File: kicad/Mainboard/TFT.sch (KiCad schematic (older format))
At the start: 2 parts, among them J6 55746-0871, Q1 BSS138

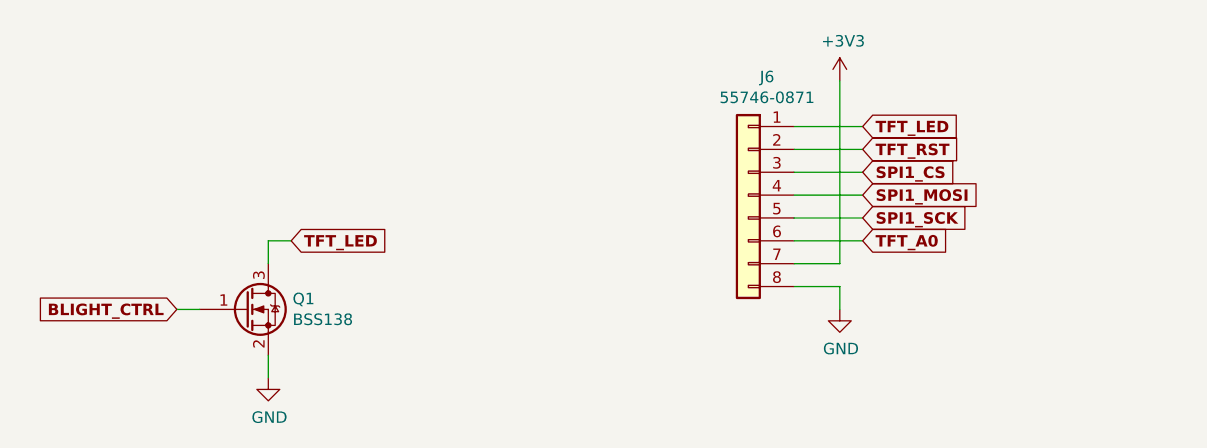
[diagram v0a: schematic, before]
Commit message: Add files via upload
* replaced Q7 with BSS138
* new HMI connector (for keypad and display)
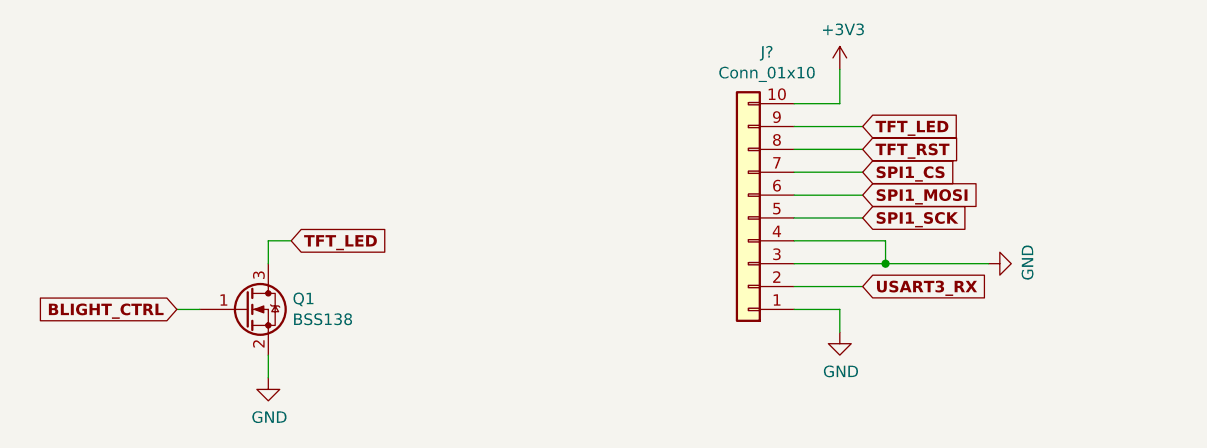
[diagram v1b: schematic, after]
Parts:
- removed J6: 55746-0871, symbol Mainboard-rescue:Conn_01x08-conn
- added J?: Conn_01x10, symbol Connector_Generic:Conn_01x10
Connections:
- net +3V3: now also J?.10 (Pin_10)
- net GND: now also J?.1 (Pin_1), J?.3 (Pin_3), J?.4 (Pin_4)
- net SPI1_CS: now also J?.7 (Pin_7)
- net SPI1_MOSI: now also J?.6 (Pin_6)
- net SPI1_SCK: now also J?.5 (Pin_5)
- net TFT_LED: now also J?.9 (Pin_9)
- net TFT_RST: now also J?.8 (Pin_8)
- new net USART3_RX: J?.2 (Pin_2)
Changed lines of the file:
@@
 EESchema Schematic File Version 4
+LIBS:Mainboard-cache
 EELAYER 30 0
 EELAYER END
@@
 encoding utf-8
 Sheet 4 7
-Title "Display Connector"
+Title "HMI Board Connector"
 Date ""
 Rev ""
@@
 Text GLabel 3600 3800 2    50   Input ~ 10
 TFT_LED
-$Comp
-L Mainboard-rescue:Conn_01x08-conn J6
-U 1 1 5DF0C355
-P 5600 3600
-F 0 "J6" H 5518 4117 50  0000 C CNN
-F 1 "55746-0871" H 5518 4026 50  0000 C CNN
-F 2 "" H 5600 3600 50  0001 C CNN
-F 3 "~" H 5600 3600 50  0001 C CNN
-	1    5600 3600
-	-1   0    0    -1
-$EndComp
 Text GLabel 6100 3300 2    50   Input ~ 10
 TFT_LED
@@
 Text GLabel 6100 3700 2    50   Input ~ 10
 SPI1_SCK
-Text GLabel 6100 3800 2    50   Input ~ 10
-TFT_A0
 Wire Wire Line
 	5800 3300 6100 3300
@@
 	5800 3700 6100 3700
 Wire Wire Line
-	5800 3800 6100 3800
+	5800 3200 6000 3200
 Wire Wire Line
-	5800 3900 6000 3900
-Wire Wire Line
-	6000 3900 6000 3100
+	6000 3200 6000 3050
 $Comp
 L power:+3V3 #PWR049
 U 1 1 5DF0DB74
-P 6000 3100
-F 0 "#PWR049" H 6000 2950 50  0001 C CNN
-F 1 "+3V3" H 6015 3273 50  0000 C CNN
-F 2 "" H 6000 3100 50  0001 C CNN
-F 3 "" H 6000 3100 50  0001 C CNN
-	1    6000 3100
+P 6000 3050
+F 0 "#PWR049" H 6000 2900 50  0001 C CNN
+F 1 "+3V3" H 6015 3223 50  0000 C CNN
+F 2 "" H 6000 3050 50  0001 C CNN
+F 3 "" H 6000 3050 50  0001 C CNN
+	1    6000 3050
 	1    0    0    -1
 $EndComp
 Wire Wire Line
-	5800 4000 6000 4000
+	5800 4100 6000 4100
 Wire Wire Line
-	6000 4000 6000 4100
+	6000 4100 6000 4200
 $Comp
 L power:GND #PWR050
 U 1 1 5DF0E0D2
-P 6000 4100
-F 0 "#PWR050" H 6000 3850 50  0001 C CNN
-F 1 "GND" H 6005 3927 50  0000 C CNN
-F 2 "" H 6000 4100 50  0001 C CNN
-F 3 "" H 6000 4100 50  0001 C CNN
-	1    6000 4100
+P 6000 4200
+F 0 "#PWR050" H 6000 3950 50  0001 C CNN
+F 1 "GND" H 6005 4027 50  0000 C CNN
+F 2 "" H 6000 4200 50  0001 C CNN
+F 3 "" H 6000 4200 50  0001 C CNN
+	1    6000 4200
 	1    0    0    -1
 $EndComp
+Wire Wire Line
+	5800 4000 6100 4000
+Text GLabel 6100 4000 2    50   Input ~ 10
+USART3_RX
+$Comp
+L power:GND #PWR?
+U 1 1 5E1E62B4
+P 6650 3900
+F 0 "#PWR?" H 6650 3650 50  0001 C CNN
+F 1 "GND" H 6655 3727 50  0000 C CNN
+F 2 "" H 6650 3900 50  0001 C CNN
+F 3 "" H 6650 3900 50  0001 C CNN
+	1    6650 3900
+	0    -1   -1   0
+$EndComp
+Wire Wire Line
+	5800 3900 6200 3900
+Wire Wire Line
+	5800 3800 6200 3800
+Wire Wire Line
+	6200 3800 6200 3900
+Connection ~ 6200 3900
+Wire Wire Line
+	6200 3900 6650 3900
+$Comp
+L Connector_Generic:Conn_01x10 J?
+U 1 1 5E1EAE64
+P 5600 3700
+F 0 "J?" H 5518 2975 50  0000 C CNN
+F 1 "Conn_01x10" H 5518 3066 50  0000 C CNN
+F 2 "" H 5600 3700 50  0001 C CNN
+F 3 "~" H 5600 3700 50  0001 C CNN
+	1    5600 3700
+	-1   0    0    1
+$EndComp
 $EndSCHEMATC

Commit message: Add files via upload
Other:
- moved on the sheet: J?, Q1
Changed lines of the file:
@@
 L Mainboard-rescue:BSS138-transistors Q1
 U 1 1 5DF0AD3D
-P 3400 4100
-F 0 "Q1" H 3606 4146 50  0000 L CNN
-F 1 "BSS138" H 3606 4055 50  0000 L CNN
-F 2 "TO_SOT_Packages_SMD:SOT-23" H 3600 4025 50  0001 L CIN
-F 3 "https://www.fairchildsemi.com/datasheets/BS/BSS138.pdf" H 3400 4100 50  0001 L CNN
-	1    3400 4100
+P 4300 3750
+F 0 "Q1" H 4506 3796 50  0000 L CNN
+F 1 "BSS138" H 4506 3705 50  0000 L CNN
+F 2 "TO_SOT_Packages_SMD:SOT-23" H 4500 3675 50  0001 L CIN
+F 3 "https://www.fairchildsemi.com/datasheets/BS/BSS138.pdf" H 4300 3750 50  0001 L CNN
+	1    4300 3750
 	1    0    0    -1
 $EndComp
@@
 L power:GND #PWR051
 U 1 1 5DF0BBF9
-P 3500 4400
-F 0 "#PWR051" H 3500 4150 50  0001 C CNN
-F 1 "GND" H 3505 4227 50  0000 C CNN
-F 2 "" H 3500 4400 50  0001 C CNN
-F 3 "" H 3500 4400 50  0001 C CNN
-	1    3500 4400
+P 4400 4050
+F 0 "#PWR051" H 4400 3800 50  0001 C CNN
+F 1 "GND" H 4405 3877 50  0000 C CNN
+F 2 "" H 4400 4050 50  0001 C CNN
+F 3 "" H 4400 4050 50  0001 C CNN
+	1    4400 4050
 	1    0    0    -1
 $EndComp
 Wire Wire Line
-	3500 4300 3500 4400
+	4400 3950 4400 4050
 Wire Wire Line
-	3200 4100 3100 4100
-Text GLabel 3100 4100 0    50   Input ~ 10
+	4100 3750 4000 3750
+Text GLabel 4000 3750 0    50   Input ~ 10
 BLIGHT_CTRL
 Wire Wire Line
-	3500 3900 3500 3800
+	4400 3550 4400 3450
 Wire Wire Line
-	3500 3800 3600 3800
-Text GLabel 3600 3800 2    50   Input ~ 10
+	4400 3450 4500 3450
+Text GLabel 4500 3450 2    50   Input ~ 10
 TFT_LED
-Text GLabel 6100 3300 2    50   Input ~ 10
+Text GLabel 6750 3450 2    50   Input ~ 10
 TFT_LED
-Text GLabel 6100 3400 2    50   Input ~ 10
+Text GLabel 6750 3550 2    50   Input ~ 10
 TFT_RST
-Text GLabel 6100 3500 2    50   Input ~ 10
+Text GLabel 6750 3650 2    50   Input ~ 10
 SPI1_CS
-Text GLabel 6100 3600 2    50   Input ~ 10
+Text GLabel 6750 3750 2    50   Input ~ 10
 SPI1_MOSI
-Text GLabel 6100 3700 2    50   Input ~ 10
+Text GLabel 6750 3850 2    50   Input ~ 10
 SPI1_SCK
 Wire Wire Line
-	5800 3300 6100 3300
+	6450 3450 6750 3450
 Wire Wire Line
-	5800 3400 6100 3400
+	6450 3550 6750 3550
 Wire Wire Line
-	5800 3500 6100 3500
+	6450 3650 6750 3650
 Wire Wire Line
-	5800 3600 6100 3600
+	6450 3750 6750 3750
 Wire Wire Line
-	5800 3700 6100 3700
+	6450 3850 6750 3850
 Wire Wire Line
-	5800 3200 6000 3200
+	6450 3350 6650 3350
 Wire Wire Line
-	6000 3200 6000 3050
+	6650 3350 6650 3200
 $Comp
 L power:+3V3 #PWR049
 U 1 1 5DF0DB74
-P 6000 3050
-F 0 "#PWR049" H 6000 2900 50  0001 C CNN
-F 1 "+3V3" H 6015 3223 50  0000 C CNN
-F 2 "" H 6000 3050 50  0001 C CNN
-F 3 "" H 6000 3050 50  0001 C CNN
-	1    6000 3050
+P 6650 3200
+F 0 "#PWR049" H 6650 3050 50  0001 C CNN
+F 1 "+3V3" H 6665 3373 50  0000 C CNN
+F 2 "" H 6650 3200 50  0001 C CNN
+F 3 "" H 6650 3200 50  0001 C CNN
+	1    6650 3200
 	1    0    0    -1
 $EndComp
 Wire Wire Line
-	5800 4100 6000 4100
+	6450 4250 6650 4250
 Wire Wire Line
-	6000 4100 6000 4200
+	6650 4250 6650 4350
 $Comp
 L power:GND #PWR050
 U 1 1 5DF0E0D2
-P 6000 4200
-F 0 "#PWR050" H 6000 3950 50  0001 C CNN
-F 1 "GND" H 6005 4027 50  0000 C CNN
-F 2 "" H 6000 4200 50  0001 C CNN
-F 3 "" H 6000 4200 50  0001 C CNN
-	1    6000 4200
+P 6650 4350
+F 0 "#PWR050" H 6650 4100 50  0001 C CNN
+F 1 "GND" H 6655 4177 50  0000 C CNN
+F 2 "" H 6650 4350 50  0001 C CNN
+F 3 "" H 6650 4350 50  0001 C CNN
+	1    6650 4350
 	1    0    0    -1
 $EndComp
 Wire Wire Line
-	5800 4000 6100 4000
-Text GLabel 6100 4000 2    50   Input ~ 10
+	6450 4150 6750 4150
+Text GLabel 6750 4150 2    50   Input ~ 10
 USART3_RX
 $Comp
 L power:GND #PWR?
 U 1 1 5E1E62B4
-P 6650 3900
-F 0 "#PWR?" H 6650 3650 50  0001 C CNN
-F 1 "GND" H 6655 3727 50  0000 C CNN
-F 2 "" H 6650 3900 50  0001 C CNN
-F 3 "" H 6650 3900 50  0001 C CNN
-	1    6650 3900
+P 7300 4050
+F 0 "#PWR?" H 7300 3800 50  0001 C CNN
+F 1 "GND" H 7305 3877 50  0000 C CNN
+F 2 "" H 7300 4050 50  0001 C CNN
+F 3 "" H 7300 4050 50  0001 C CNN
+	1    7300 4050
 	0    -1   -1   0
 $EndComp
 Wire Wire Line
-	5800 3900 6200 3900
+	6450 4050 6850 4050
 Wire Wire Line
-	5800 3800 6200 3800
+	6450 3950 6850 3950
 Wire Wire Line
-	6200 3800 6200 3900
-Connection ~ 6200 3900
+	6850 3950 6850 4050
+Connection ~ 6850 4050
 Wire Wire Line
-	6200 3900 6650 3900
+	6850 4050 7300 4050
 $Comp
 L Connector_Generic:Conn_01x10 J?
 U 1 1 5E1EAE64
-P 5600 3700
-F 0 "J?" H 5518 2975 50  0000 C CNN
-F 1 "Conn_01x10" H 5518 3066 50  0000 C CNN
-F 2 "" H 5600 3700 50  0001 C CNN
-F 3 "~" H 5600 3700 50  0001 C CNN
-	1    5600 3700
+P 6250 3850
+F 0 "J?" H 6168 3125 50  0000 C CNN
+F 1 "Conn_01x10" H 6168 3216 50  0000 C CNN
+F 2 "" H 6250 3850 50  0001 C CNN
+F 3 "~" H 6250 3850 50  0001 C CNN
+	1    6250 3850
 	-1   0    0    1
 $EndComp

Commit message: Add files via upload
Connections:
- net USART3_RX renamed UART7_RX
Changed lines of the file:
@@
 $Descr A4 11693 8268
 encoding utf-8
-Sheet 4 7
+Sheet 4 8
 Title "HMI Board Connector"
 Date ""
@@
 	6450 4150 6750 4150
 Text GLabel 6750 4150 2    50   Input ~ 10
-USART3_RX
+UART7_RX
 $Comp
 L power:GND #PWR?

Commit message: Annotated parts, again.
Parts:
- gave numbers to parts that had none: 1
- renumbered Q1 to Q2
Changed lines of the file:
@@
 EESchema Schematic File Version 4
-LIBS:Mainboard-cache
 EELAYER 30 0
 EELAYER END
@@
 $EndDescr
 $Comp
-L Mainboard-rescue:BSS138-transistors Q1
+L Mainboard-rescue:BSS138-transistors Q2
 U 1 1 5DF0AD3D
 P 4300 3750
-F 0 "Q1" H 4506 3796 50  0000 L CNN
+F 0 "Q2" H 4506 3796 50  0000 L CNN
 F 1 "BSS138" H 4506 3705 50  0000 L CNN
 F 2 "TO_SOT_Packages_SMD:SOT-23" H 4500 3675 50  0001 L CIN
@@
 	6650 3350 6650 3200
 $Comp
-L power:+3V3 #PWR049
+L power:+3V3 #PWR052
 U 1 1 5DF0DB74
 P 6650 3200
-F 0 "#PWR049" H 6650 3050 50  0001 C CNN
+F 0 "#PWR052" H 6650 3050 50  0001 C CNN
 F 1 "+3V3" H 6665 3373 50  0000 C CNN
 F 2 "" H 6650 3200 50  0001 C CNN
@@
 	6650 4250 6650 4350
 $Comp
-L power:GND #PWR050
+L power:GND #PWR053
 U 1 1 5DF0E0D2
 P 6650 4350
-F 0 "#PWR050" H 6650 4100 50  0001 C CNN
+F 0 "#PWR053" H 6650 4100 50  0001 C CNN
 F 1 "GND" H 6655 4177 50  0000 C CNN
 F 2 "" H 6650 4350 50  0001 C CNN
@@
 UART7_RX
 $Comp
-L power:GND #PWR?
+L power:GND #PWR054
 U 1 1 5E1E62B4
 P 7300 4050
-F 0 "#PWR?" H 7300 3800 50  0001 C CNN
+F 0 "#PWR054" H 7300 3800 50  0001 C CNN
 F 1 "GND" H 7305 3877 50  0000 C CNN
 F 2 "" H 7300 4050 50  0001 C CNN
@@
 	6850 4050 7300 4050
 $Comp
-L Connector_Generic:Conn_01x10 J?
+L Connector_Generic:Conn_01x10 J7
 U 1 1 5E1EAE64
 P 6250 3850
-F 0 "J?" H 6168 3125 50  0000 C CNN
+F 0 "J7" H 6168 3125 50  0000 C CNN
 F 1 "Conn_01x10" H 6168 3216 50  0000 C CNN
 F 2 "" H 6250 3850 50  0001 C CNN

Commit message: Started assigning footprints
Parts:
- J7: symbol Connector_Generic:Conn_01x10 -> Mainboard-rescue:Conn_01x10-Connector_Generic
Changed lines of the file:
@@
 	6850 4050 7300 4050
 $Comp
-L Connector_Generic:Conn_01x10 J7
+L Mainboard-rescue:Conn_01x10-Connector_Generic J7
 U 1 1 5E1EAE64
 P 6250 3850
